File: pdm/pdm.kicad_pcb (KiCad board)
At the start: 4 copper layers, 129.5 x 99.1 mm, 107 parts, among them J1 Conn_01x04_Male, J2 Conn_01x12_Male, J3 Conn_01x08_Male, Q1 MMBT3904, Q10 Q_NPN_BCE, Q2 Q_NPN_BCE, Q3 MMBT3904, Q4 Q_NPN_BCE, Q5 MMBT3904, Q6 Q_NPN_BCE, Q7 MMBT3904, Q8 Q_NPN_BCE, Q9 MMBT3904, SW1 SW_Push, U1 AZ1117CH-3_3TRG1, U2 SN65HVD233, U3 STM32F042G6Ux, U4 BTS443P, U5 BTS443P, U6 BTS443P, U7 BTS443P, U8 BTS443P

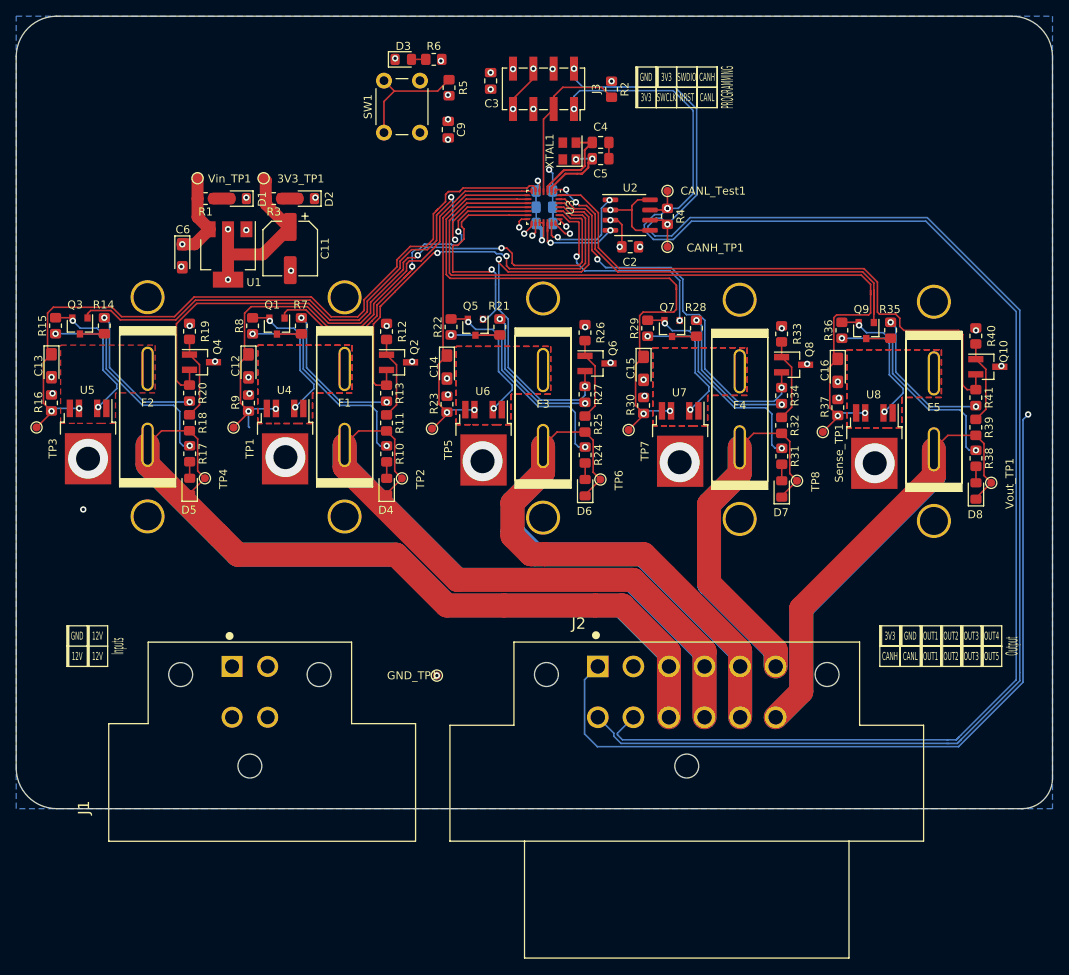
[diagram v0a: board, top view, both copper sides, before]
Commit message: fixed issues #3 & #5
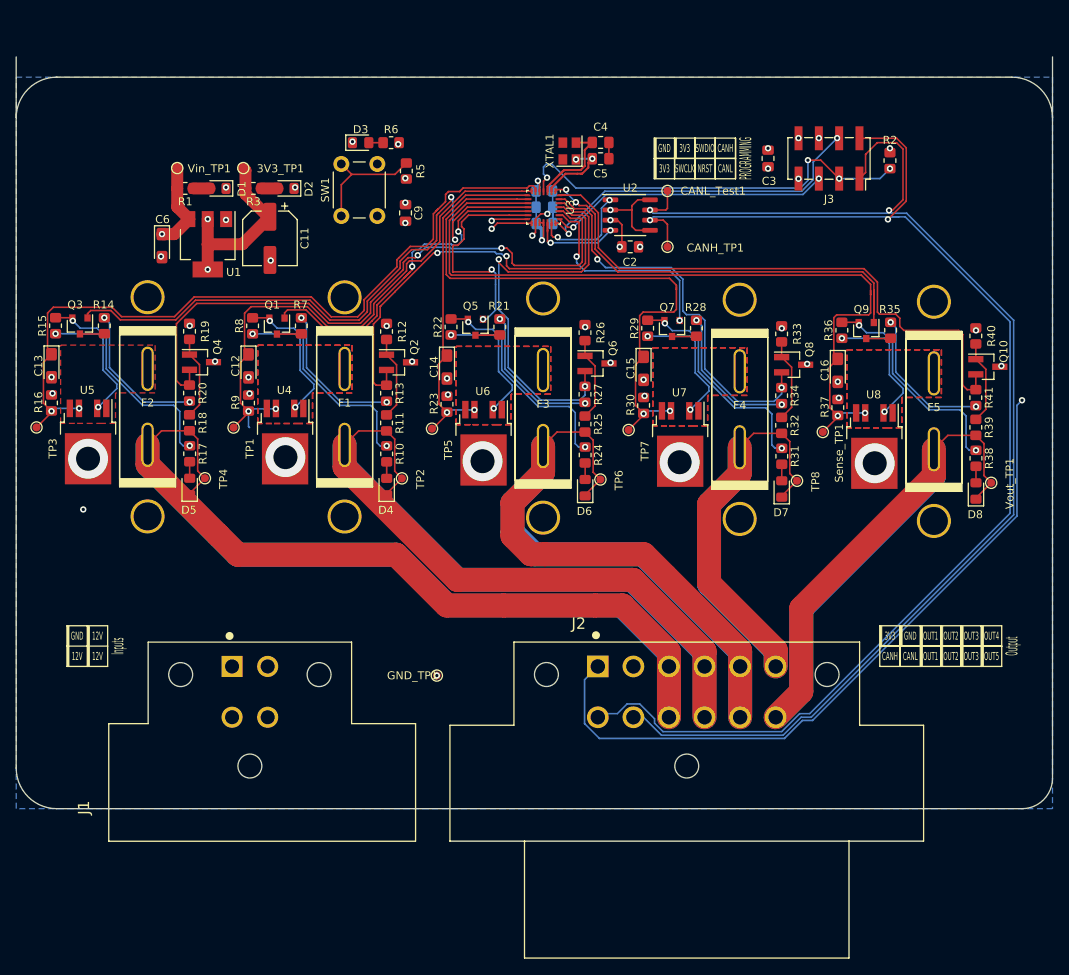
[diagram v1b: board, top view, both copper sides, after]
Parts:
- removed R4: 120R, Resistor_SMD:R_0805_2012Metric_Pad1.20x1.40mm_HandSolder
- moved J3 36.7 mm to (205.9, 58.7)
- moved C3 36.0 mm to (198.2, 58.7)
- moved R2 35.9 mm to (213.5, 58.9)
- moved C9 11.7 mm to (152.9, 65.5)
- moved D3 11.7 mm to (147.3, 56.7)
- moved R5 11.7 mm to (153.0, 60.2)
- moved R6 11.7 mm to (151.1, 56.7)
- moved SW1 11.7 mm to (144.9, 65.9)
- moved D2 2.84 mm to (138.0, 62.4)
- moved D1 2.84 mm to (129.5, 62.4)
- moved C6 2.84 mm to (122.5, 69.6)
- moved 3V3_TP1 2.84 mm to (132.7, 59.9)
- moved R3 2.84 mm to (133.9, 62.4)
- moved Vin_TP1 2.84 mm to (124.4, 59.9)
- moved C11 2.84 mm to (136.0, 68.7)
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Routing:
- net /_N: track 196.9 -> 157.9 mm, vias 3 -> 2
- net /_P: track 201.1 -> 162.7 mm
- net /NRST: track 20.7 -> 52.5 mm, vias 0 -> 4
- net /SWDIO: track 24.5 -> 43.3 mm
- net +3V3: track 240.0 -> 221.5 mm
- net /SWCLK: track 18.5 -> 35.4 mm
- net /LED_DEBUG: track 31.5 -> 24.0 mm
- net +12V: track 57.6 -> 55.6 mm
- net /DEBUG_BUTTON: track 43.4 -> 44.7 mm
- net GND: track 26.7 -> 27.9 mm
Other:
- board size 129.5 x 99.1 mm -> 129.5 x 94 mm

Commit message: added block labels as per issue #4
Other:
- board size 129.5 x 94 mm -> 129.5 x 91.4 mm
- board text added: "BLOCK 1"
- board text added: "BLOCK 2"
- board text added: "BLOCK 3"
- board text added: "BLOCK 4"
- board text added: "BLOCK 5"
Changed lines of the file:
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@@
   (general
     (thickness 1.6)
-    (drawings 148)
+    (drawings 153)
     (tracks 1111)
     (zones 0)
@@
     )
   )
+  (gr_text "BLOCK 5" (at 219.202 108.204) (layer F.SilkS)
+    (effects (font (size 1.5 1.5) (thickness 0.3)))
+  )
+  (gr_text "BLOCK 4" (at 194.437 108.204) (layer F.SilkS)
+    (effects (font (size 1.5 1.5) (thickness 0.3)))
+  )
+  (gr_text "BLOCK 3" (at 170.307 108.204) (layer F.SilkS)
+    (effects (font (size 1.5 1.5) (thickness 0.3)))
+  )
+  (gr_text "BLOCK 2" (at 145.542 108.204) (layer F.SilkS)
+    (effects (font (size 1.5 1.5) (thickness 0.3)))
+  )
+  (gr_text "BLOCK 1" (at 120.777 108.204) (layer F.SilkS)
+    (effects (font (size 1.5 1.5) (thickness 0.3)))
+  )
   (dimension 110.110007 (width 0.15) (layer Dwgs.User)
     (gr_text "110.110 mm" (at 89.017011 103.597615 -89.97918599) (layer Dwgs.User)
@@
   (gr_arc (start 229.997 136.144) (end 229.997 139.954) (angle -90) (layer Edge.Cuts) (width 0.05))
   (gr_arc (start 109.347 134.874) (end 104.267 134.874) (angle -90) (layer Edge.Cuts) (width 0.05))
-  (gr_line (start 233.807 45.974) (end 233.807 136.144) (layer Edge.Cuts) (width 0.05))
+  (gr_line (start 233.807 53.594) (end 233.807 136.144) (layer Edge.Cuts) (width 0.05))
   (gr_line (start 109.347 48.514) (end 228.727 48.514) (layer Edge.Cuts) (width 0.05))
-  (gr_line (start 104.267 134.874) (end 104.267 45.974) (layer Edge.Cuts) (width 0.05))
+  (gr_line (start 104.267 134.874) (end 104.267 53.594) (layer Edge.Cuts) (width 0.05))
   (gr_line (start 229.997 139.954) (end 109.347 139.954) (layer Edge.Cuts) (width 0.05))
   (via (at 156.845 123.317) (size 0.8) (drill 0.4) (layers F.Cu B.Cu) (net 1))

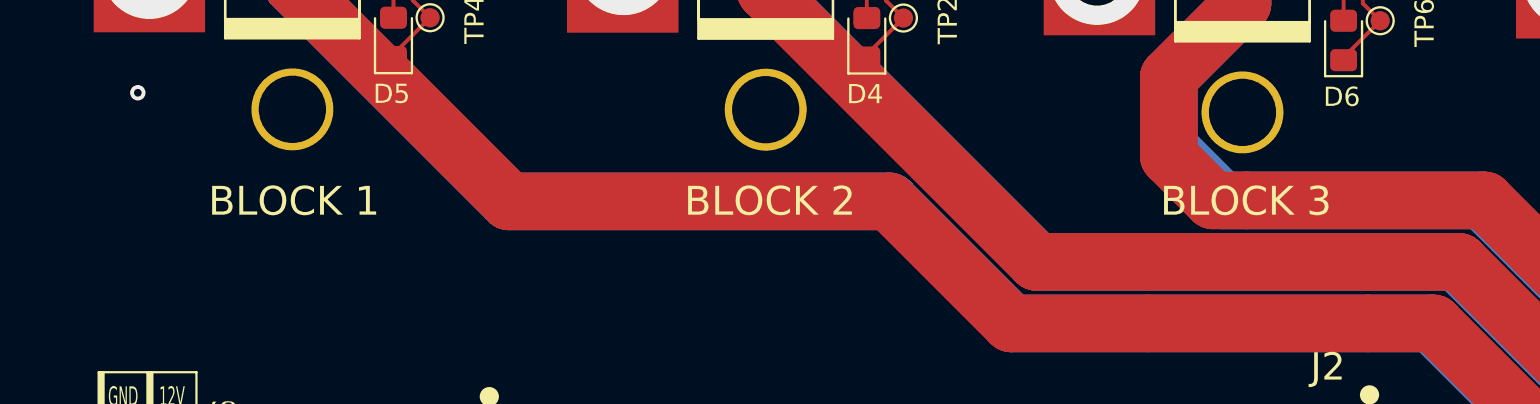
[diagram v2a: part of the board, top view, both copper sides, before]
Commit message: added high current labels for issue #4
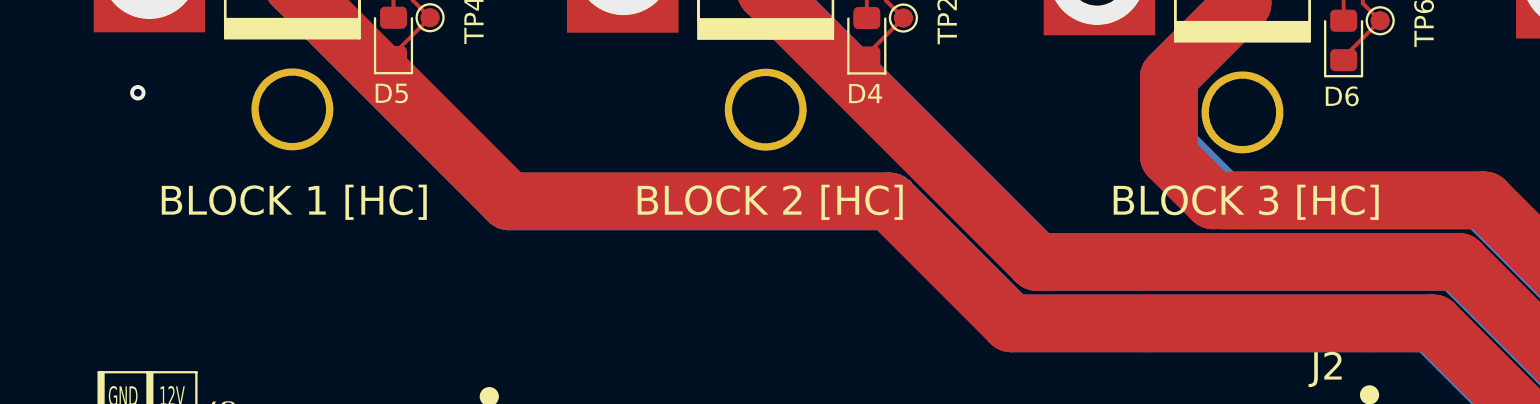
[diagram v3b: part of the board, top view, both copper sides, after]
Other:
- board text added: "BLOCK 1 [HC]"
- board text added: "BLOCK 2 [HC]"
- board text added: "BLOCK 3 [HC]"
- board text removed: "BLOCK 1"
- board text removed: "BLOCK 2"
- board text removed: "BLOCK 3"
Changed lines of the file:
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@@
     (effects (font (size 1.5 1.5) (thickness 0.3)))
   )
-  (gr_text "BLOCK 3" (at 170.307 108.204) (layer F.SilkS)
+  (gr_text "BLOCK 3 [HC]" (at 170.307 108.204) (layer F.SilkS)
     (effects (font (size 1.5 1.5) (thickness 0.3)))
   )
-  (gr_text "BLOCK 2" (at 145.542 108.204) (layer F.SilkS)
+  (gr_text "BLOCK 2 [HC]" (at 145.542 108.204) (layer F.SilkS)
     (effects (font (size 1.5 1.5) (thickness 0.3)))
   )
-  (gr_text "BLOCK 1" (at 120.777 108.204) (layer F.SilkS)
+  (gr_text "BLOCK 1 [HC]" (at 120.777 108.204) (layer F.SilkS)
     (effects (font (size 1.5 1.5) (thickness 0.3)))
   )

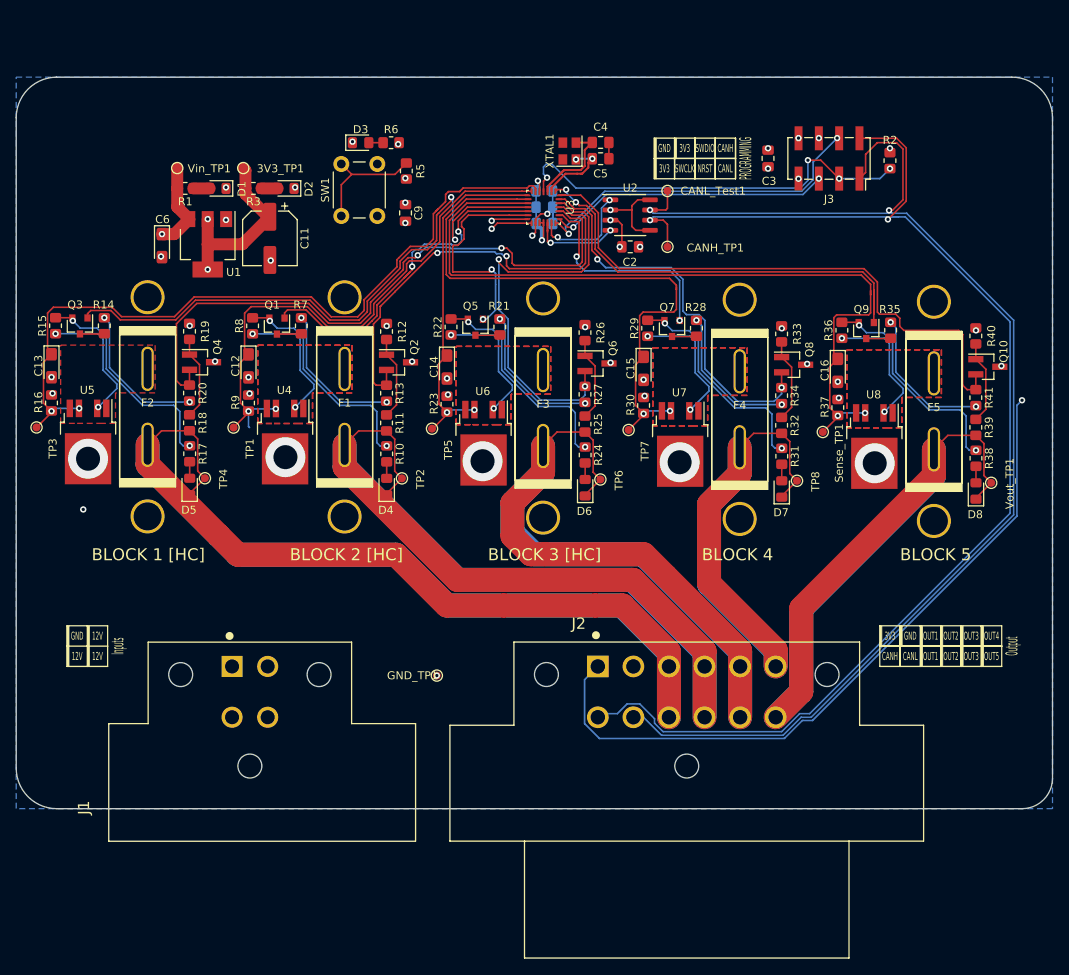
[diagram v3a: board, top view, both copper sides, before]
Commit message: added mounting holes as per issue #2
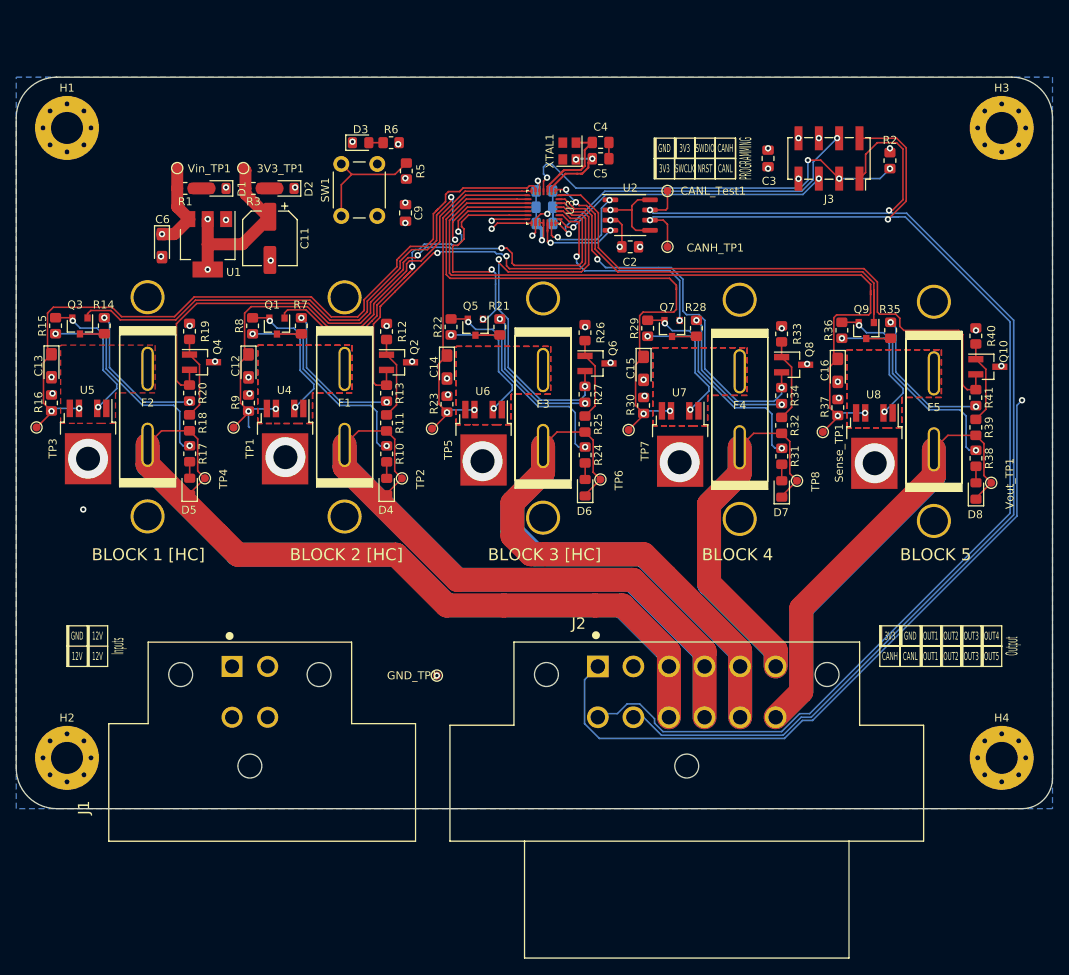
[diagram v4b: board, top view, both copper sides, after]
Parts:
- added H1: MountingHole, MountingHole:MountingHole_4mm_Pad_Via, F.Cu at (110.6, 54.9)
- added H2: MountingHole, MountingHole:MountingHole_4mm_Pad_Via, F.Cu at (110.6, 133.6)
- added H3: MountingHole, MountingHole:MountingHole_4mm_Pad_Via, F.Cu at (227.5, 54.9)
- added H4: MountingHole, MountingHole:MountingHole_4mm_Pad_Via, F.Cu at (227.5, 133.6)
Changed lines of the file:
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@@
     (tracks 1111)
     (zones 0)
-    (modules 106)
+    (modules 110)
     (nets 69)
   )
@@
     (add_net +12V)
   )
+  (module MountingHole:MountingHole_4mm_Pad_Via (layer F.Cu)
+    (at 227.457 133.604)
+    (descr "Mounting Hole 4mm")
+    (tags "mounting hole 4mm")
+    (attr virtual)
+    (fp_text reference H4 (at 0 -5) (layer F.SilkS)
+      (effects (font (size 1 1) (thickness 0.15)))
+    )
+    (fp_text value MountingHole (at 0 5) (layer F.Fab)
+      (effects (font (size 1 1) (thickness 0.15)))
+    )
+    (fp_text user %R (at 0.3 0) (layer F.Fab)
+      (effects (font (size 1 1) (thickness 0.15)))
+    )
+    (fp_circle (center 0 0) (end 4 0) (layer Cmts.User) (width 0.15))
+    (fp_circle (center 0 0) (end 4.25 0) (layer F.CrtYd) (width 0.05))
+    (pad 1 thru_hole circle (at 2.12132 -2.12132) (size 0.9 0.9) (drill 0.6) (layers *.Cu *.Mask))
+    (pad 1 thru_hole circle (at 0 -3) (size 0.9 0.9) (drill 0.6) (layers *.Cu *.Mask))
+    (pad 1 thru_hole circle (at -2.12132 -2.12132) (size 0.9 0.9) (drill 0.6) (layers *.Cu *.Mask))
+    (pad 1 thru_hole circle (at -3 0) (size 0.9 0.9) (drill 0.6) (layers *.Cu *.Mask))
+    (pad 1 thru_hole circle (at -2.12132 2.12132) (size 0.9 0.9) (drill 0.6) (layers *.Cu *.Mask))
+    (pad 1 thru_hole circle (at 0 3) (size 0.9 0.9) (drill 0.6) (layers *.Cu *.Mask))
+    (pad 1 thru_hole circle (at 2.12132 2.12132) (size 0.9 0.9) (drill 0.6) (layers *.Cu *.Mask))
+    (pad 1 thru_hole circle (at 3 0) (size 0.9 0.9) (drill 0.6) (layers *.Cu *.Mask))
+    (pad 1 thru_hole circle (at 0 0) (size 8 8) (drill 4) (layers *.Cu *.Mask))
+  )
+  (module MountingHole:MountingHole_4mm_Pad_Via (layer F.Cu)
+    (at 227.457 54.864)
+    (descr "Mounting Hole 4mm")
+    (tags "mounting hole 4mm")
+    (attr virtual)
+    (fp_text reference H3 (at 0 -5) (layer F.SilkS)
+      (effects (font (size 1 1) (thickness 0.15)))
+    )
+    (fp_text value MountingHole (at 0 5) (layer F.Fab)
+      (effects (font (size 1 1) (thickness 0.15)))
+    )
+    (fp_text user %R (at 0.3 0) (layer F.Fab)
+      (effects (font (size 1 1) (thickness 0.15)))
+    )
+    (fp_circle (center 0 0) (end 4 0) (layer Cmts.User) (width 0.15))
+    (fp_circle (center 0 0) (end 4.25 0) (layer F.CrtYd) (width 0.05))
+    (pad 1 thru_hole circle (at 2.12132 -2.12132) (size 0.9 0.9) (drill 0.6) (layers *.Cu *.Mask))
+    (pad 1 thru_hole circle (at 0 -3) (size 0.9 0.9) (drill 0.6) (layers *.Cu *.Mask))
+    (pad 1 thru_hole circle (at -2.12132 -2.12132) (size 0.9 0.9) (drill 0.6) (layers *.Cu *.Mask))
+    (pad 1 thru_hole circle (at -3 0) (size 0.9 0.9) (drill 0.6) (layers *.Cu *.Mask))
+    (pad 1 thru_hole circle (at -2.12132 2.12132) (size 0.9 0.9) (drill 0.6) (layers *.Cu *.Mask))
+    (pad 1 thru_hole circle (at 0 3) (size 0.9 0.9) (drill 0.6) (layers *.Cu *.Mask))
+    (pad 1 thru_hole circle (at 2.12132 2.12132) (size 0.9 0.9) (drill 0.6) (layers *.Cu *.Mask))
+    (pad 1 thru_hole circle (at 3 0) (size 0.9 0.9) (drill 0.6) (layers *.Cu *.Mask))
+    (pad 1 thru_hole circle (at 0 0) (size 8 8) (drill 4) (layers *.Cu *.Mask))
+  )
+  (module MountingHole:MountingHole_4mm_Pad_Via (layer F.Cu)
+    (at 110.617 133.604)
+    (descr "Mounting Hole 4mm")
+    (tags "mounting hole 4mm")
+    (attr virtual)
+    (fp_text reference H2 (at 0 -5) (layer F.SilkS)
+      (effects (font (size 1 1) (thickness 0.15)))
+    )
+    (fp_text value MountingHole (at 0 5) (layer F.Fab)
+      (effects (font (size 1 1) (thickness 0.15)))
+    )
+    (fp_text user %R (at 0.3 0) (layer F.Fab)
+      (effects (font (size 1 1) (thickness 0.15)))
+    )
+    (fp_circle (center 0 0) (end 4 0) (layer Cmts.User) (width 0.15))
+    (fp_circle (center 0 0) (end 4.25 0) (layer F.CrtYd) (width 0.05))
+    (pad 1 thru_hole circle (at 2.12132 -2.12132) (size 0.9 0.9) (drill 0.6) (layers *.Cu *.Mask))
+    (pad 1 thru_hole circle (at 0 -3) (size 0.9 0.9) (drill 0.6) (layers *.Cu *.Mask))
+    (pad 1 thru_hole circle (at -2.12132 -2.12132) (size 0.9 0.9) (drill 0.6) (layers *.Cu *.Mask))
+    (pad 1 thru_hole circle (at -3 0) (size 0.9 0.9) (drill 0.6) (layers *.Cu *.Mask))
+    (pad 1 thru_hole circle (at -2.12132 2.12132) (size 0.9 0.9) (drill 0.6) (layers *.Cu *.Mask))
+    (pad 1 thru_hole circle (at 0 3) (size 0.9 0.9) (drill 0.6) (layers *.Cu *.Mask))
+    (pad 1 thru_hole circle (at 2.12132 2.12132) (size 0.9 0.9) (drill 0.6) (layers *.Cu *.Mask))
+    (pad 1 thru_hole circle (at 3 0) (size 0.9 0.9) (drill 0.6) (layers *.Cu *.Mask))
+    (pad 1 thru_hole circle (at 0 0) (size 8 8) (drill 4) (layers *.Cu *.Mask))
+  )
+  (module MountingHole:MountingHole_4mm_Pad_Via (layer F.Cu)
+    (at 110.617 54.864)
+    (descr "Mounting Hole 4mm")
+    (tags "mounting hole 4mm")
+    (attr virtual)
+    (fp_text reference H1 (at 0 -5) (layer F.SilkS)
+      (effects (font (size 1 1) (thickness 0.15)))
+    )
+    (fp_text value MountingHole (at 0 5) (layer F.Fab)
+      (effects (font (size 1 1) (thickness 0.15)))
+    )
+    (fp_text user %R (at 0.3 0) (layer F.Fab)
+      (effects (font (size 1 1) (thickness 0.15)))
+    )
+    (fp_circle (center 0 0) (end 4 0) (layer Cmts.User) (width 0.15))
+    (fp_circle (center 0 0) (end 4.25 0) (layer F.CrtYd) (width 0.05))
+    (pad 1 thru_hole circle (at 2.12132 -2.12132) (size 0.9 0.9) (drill 0.6) (layers *.Cu *.Mask))
+    (pad 1 thru_hole circle (at 0 -3) (size 0.9 0.9) (drill 0.6) (layers *.Cu *.Mask))
+    (pad 1 thru_hole circle (at -2.12132 -2.12132) (size 0.9 0.9) (drill 0.6) (layers *.Cu *.Mask))
+    (pad 1 thru_hole circle (at -3 0) (size 0.9 0.9) (drill 0.6) (layers *.Cu *.Mask))
+    (pad 1 thru_hole circle (at -2.12132 2.12132) (size 0.9 0.9) (drill 0.6) (layers *.Cu *.Mask))
+    (pad 1 thru_hole circle (at 0 3) (size 0.9 0.9) (drill 0.6) (layers *.Cu *.Mask))
+    (pad 1 thru_hole circle (at 2.12132 2.12132) (size 0.9 0.9) (drill 0.6) (layers *.Cu *.Mask))
+    (pad 1 thru_hole circle (at 3 0) (size 0.9 0.9) (drill 0.6) (layers *.Cu *.Mask))
+    (pad 1 thru_hole circle (at 0 0) (size 8 8) (drill 4) (layers *.Cu *.Mask))
+  )
   (module Oscillator:Oscillator_SMD_Abracon_ASE-4Pin_3.2x2.5mm (layer F.Cu)

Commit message: added pepe as per issue #1
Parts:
- added G***: LOGO, pdm_v2:rarepepe, F.Cu at (149.7, 109.5)
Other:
- board text added: "PCB By Henry Chen"
- board text added: "PDM Board V1.0"
- board text added: "“mixed feels”"
